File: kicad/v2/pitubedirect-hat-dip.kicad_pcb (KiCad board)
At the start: 2 copper layers, 57 x 65 mm, 13 parts, among them P1 CONN_02X20, P2 CONN_02X20, P3 CONN_01X02, P4 CONN_01X03, U1 74LVC245AN, U2 74LVC245AN

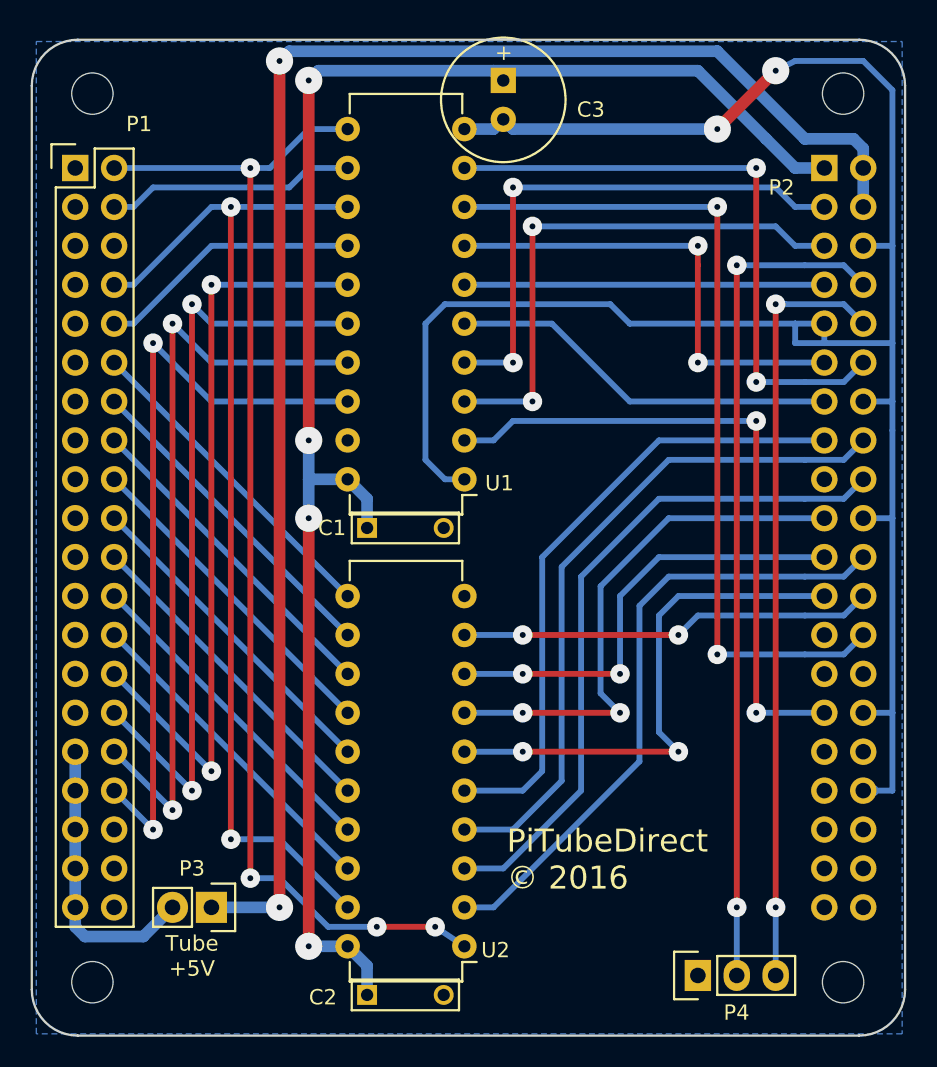
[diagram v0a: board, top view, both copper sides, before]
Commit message: Some final adjustments to v2 PCB
Change-Id: Ib4c029b2e971b775e47e1c07a81c8510d859d0c3
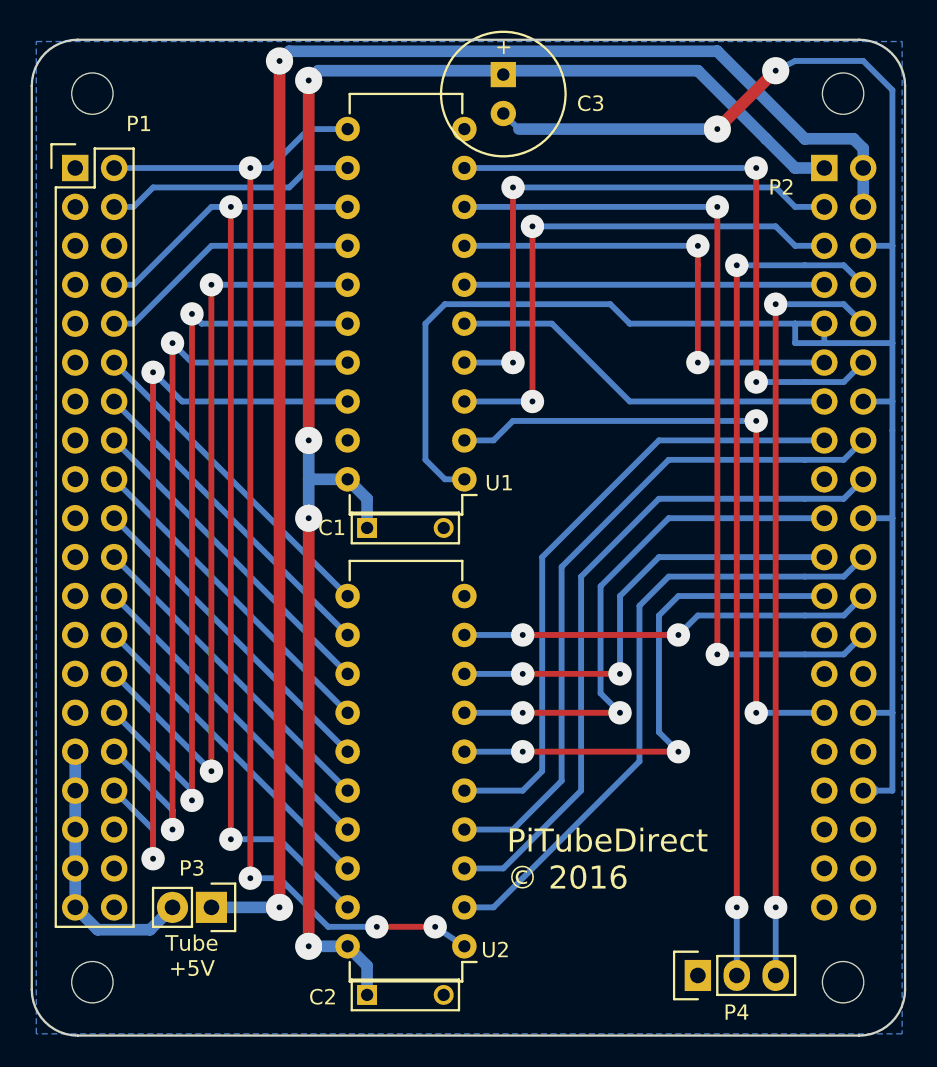
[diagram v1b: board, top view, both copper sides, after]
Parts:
- moved C3 0.38 mm to (103.5, 112.6)
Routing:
- net GND: track 134.2 -> 131.5 mm
- net /TA3: track 49.6 -> 50.7 mm
- net +5V: track 18.8 -> 17.7 mm
- net /TA2: track 49.6 -> 50.4 mm
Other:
- net class Default: via_dia 1.27 -> 1.524
